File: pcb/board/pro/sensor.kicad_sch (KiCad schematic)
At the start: 2 parts, among them U1 AH49HSC

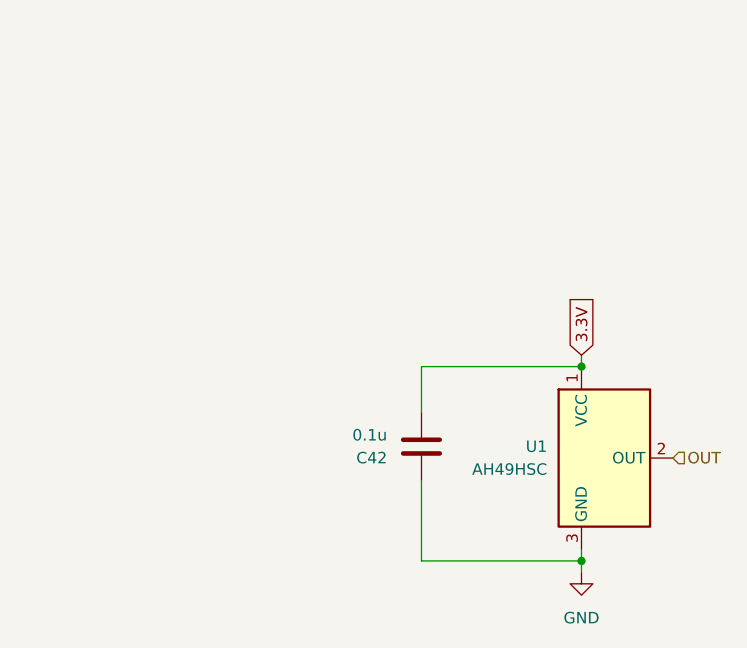
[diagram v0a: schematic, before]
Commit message: Update PCB with HSE oscillator, Footprint Mismatch fix and Rename project files to Wonkle (#36)
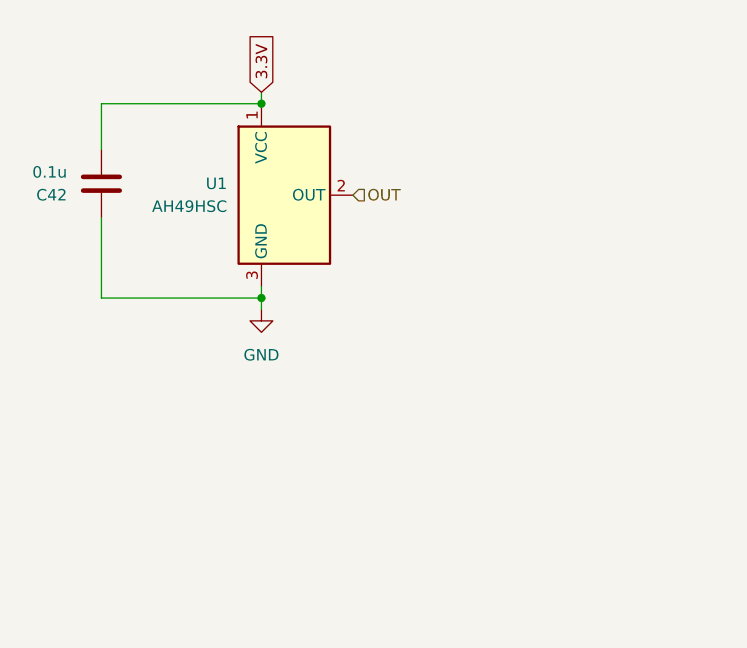
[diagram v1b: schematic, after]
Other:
- moved on the sheet: C42, U1
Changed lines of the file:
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@@
 (kicad_sch
-	(version 20250114)
+	(version 20260306)
 	(generator "eeschema")
-	(generator_version "9.0")
-	(paper "A5")
+	(generator_version "10.0")
+	(paper "User" 135 110)
 	(junction
-		(at 104.14 80.01)
+		(at 68.58 50.8)
 		(diameter 0)
 		(color 0 0 0 0)
 	)
 	(junction
-		(at 104.14 58.42)
+		(at 68.58 29.21)
 		(diameter 0)
 		(color 0 0 0 0)
@@
 	(wire
 		(pts
-			(xy 104.14 80.01) (xy 104.14 78.74)
+			(xy 68.58 50.8) (xy 68.58 49.53)
 		)
 		(stroke
@@
 	(wire
 		(pts
-			(xy 86.36 58.42) (xy 104.14 58.42)
+			(xy 50.8 29.21) (xy 68.58 29.21)
 		)
 		(stroke
@@
 	(wire
 		(pts
-			(xy 104.14 57.15) (xy 104.14 58.42)
+			(xy 68.58 27.94) (xy 68.58 29.21)
 		)
 		(stroke
@@
 	(wire
 		(pts
-			(xy 86.36 80.01) (xy 104.14 80.01)
+			(xy 50.8 50.8) (xy 68.58 50.8)
 		)
 		(stroke
@@
 	(wire
 		(pts
-			(xy 86.36 71.12) (xy 86.36 80.01)
+			(xy 50.8 41.91) (xy 50.8 50.8)
 		)
 		(stroke
@@
 	(wire
 		(pts
-			(xy 104.14 81.28) (xy 104.14 80.01)
+			(xy 68.58 52.07) (xy 68.58 50.8)
 		)
 		(stroke
@@
 	(wire
 		(pts
-			(xy 86.36 63.5) (xy 86.36 58.42)
+			(xy 50.8 34.29) (xy 50.8 29.21)
 		)
 		(stroke
@@
 	(global_label "3.3V"
 		(shape input)
-		(at 104.14 57.15 90)
+		(at 68.58 27.94 90)
 		(fields_autoplaced yes)
 		(effects
@@
 		)
 		(property "Intersheetrefs" "${INTERSHEET_REFS}"
-			(at 104.14 50.0524 90)
+			(at 68.58 20.8424 90)
+			(hide yes)
+			(show_name no)
+			(do_not_autoplace no)
 			(effects
 				(font
@@
 				)
 				(justify left)
-				(hide yes)
 			)
 		)
@@
 	(hierarchical_label "OUT"
 		(shape input)
-		(at 114.3 68.58 0)
+		(at 78.74 39.37 0)
 		(effects
 			(font
@@
 	(symbol
 		(lib_id "Device:C")
-		(at 86.36 67.31 180)
+		(at 50.8 38.1 180)
 		(unit 1)
+		(body_style 1)
 		(exclude_from_sim no)
 		(in_bom yes)
 		(on_board yes)
+		(in_pos_files yes)
 		(dnp no)
 		(property "Reference" "C42"
-			(at 82.55 68.5801 0)
+			(at 46.99 39.3701 0)
+			(show_name no)
+			(do_not_autoplace no)
 			(effects
 				(font
@@
 		)
 		(property "Value" "0.1u"
-			(at 82.55 66.0401 0)
+			(at 46.99 36.8301 0)
+			(show_name no)
+			(do_not_autoplace no)
 			(effects
 				(font
@@
 		)
 		(property "Footprint" "Capacitor_SMD:C_0402_1005Metric"
-			(at 85.3948 63.5 0)
+			(at 49.8348 34.29 0)
+			(hide yes)
+			(show_name no)
+			(do_not_autoplace no)
 			(effects
 				(font
 					(size 1.27 1.27)
 				)
-				(hide yes)
-			)
-		)
-		(property "Datasheet" "~"
-			(at 86.36 67.31 0)
+			)
+		)
+		(property "Datasheet" ""
+			(at 50.8 38.1 0)
+			(hide yes)
+			(show_name no)
+			(do_not_autoplace no)
 			(effects
 				(font
 					(size 1.27 1.27)
 				)
-				(hide yes)
 			)
 		)
 		(property "Description" "Unpolarized capacitor"
-			(at 86.36 67.31 0)
+			(at 50.8 38.1 0)
+			(hide yes)
+			(show_name no)
+			(do_not_autoplace no)
 			(effects
 				(font
 					(size 1.27 1.27)
 				)
-				(hide yes)
 			)
 		)
 		(property "LCSC Part #" "C1525"
-			(at 86.36 67.31 0)
+			(at 50.8 38.1 0)
+			(hide yes)
+			(show_name no)
+			(do_not_autoplace no)
 			(effects
 				(font
 					(size 1.27 1.27)
 				)
-				(hide yes)
 			)
 		)
@@
 		)
 		(instances
-			(project "pompyboard"
+			(project "Wonkle"
 				(path "/e5830f2e-b6bc-440e-bdf9-7651ab21e3a0/026cd3d2-ee49-4aa8-a6be-1ded8cec01b6/04e242d3-4b8b-4c59-b96a-ded88d9c121e"
 					(reference "C123")
@@
 	(symbol
 		(lib_id "Sensor_Magnetic:DRV5055A4xDBZxQ1")
-		(at 106.68 68.58 0)
+		(at 71.12 39.37 0)
 		(unit 1)
+		(body_style 1)
 		(exclude_from_sim no)
 		(in_bom yes)
 		(on_board yes)
+		(in_pos_files yes)
 		(dnp no)
 		(fields_autoplaced yes)
 		(property "Reference" "U1"
-			(at 100.33 67.3099 0)
+			(at 64.77 38.0999 0)
+			(show_name no)
+			(do_not_autoplace no)
 			(effects
 				(font
@@
 		)
 		(property "Value" "AH49HSC"
-			(at 100.33 69.8499 0)
+			(at 64.77 40.6399 0)
+			(show_name no)
+			(do_not_autoplace no)
 			(effects
 				(font
@@
 		)
 		(property "Footprint" "Package_TO_SOT_SMD:SOT-23-3"
-			(at 106.68 68.58 0)
+			(at 71.12 39.37 0)
+			(hide yes)
+			(show_name no)
+			(do_not_autoplace no)
 			(effects
 				(font
 					(size 1.27 1.27)
 				)
-				(hide yes)
 			)
 		)
 		(property "Datasheet" ""
-			(at 106.68 68.58 0)
+			(at 71.12 39.37 0)
+			(hide yes)
+			(show_name no)
+			(do_not_autoplace no)
 			(effects
 				(font
 					(size 1.27 1.27)
 				)
-				(hide yes)
 			)
 		)
 		(property "Description" ""
-			(at 106.68 68.58 0)
+			(at 71.12 39.37 0)
+			(hide yes)
+			(show_name no)
+			(do_not_autoplace no)
 			(effects
 				(font
 					(size 1.27 1.27)
 				)
-				(hide yes)
 			)
 		)
 		(property "LCSC Part #" "C510723"
-			(at 106.68 68.58 0)
+			(at 71.12 39.37 0)
+			(hide yes)
+			(show_name no)
+			(do_not_autoplace no)
 			(effects
 				(font
 					(size 1.27 1.27)
 				)
-				(hide yes)
 			)
 		)
@@
 		)
 		(instances
-			(project "pompyboard"
+			(project "Wonkle"
 				(path "/e5830f2e-b6bc-440e-bdf9-7651ab21e3a0/026cd3d2-ee49-4aa8-a6be-1ded8cec01b6/04e242d3-4b8b-4c59-b96a-ded88d9c121e"
 					(reference "U141")
@@
 	(symbol
 		(lib_id "power:GND")
-		(at 104.14 81.28 0)
+		(at 68.58 52.07 0)
 		(unit 1)
+		(body_style 1)
 		(exclude_from_sim no)
 		(in_bom yes)
 		(on_board yes)
+		(in_pos_files yes)
 		(dnp no)
 		(fields_autoplaced yes)
 		(property "Reference" "#PWR040"
-			(at 104.14 87.63 0)
+			(at 68.58 58.42 0)
+			(hide yes)
+			(show_name no)
+			(do_not_autoplace no)
 			(effects
 				(font
 					(size 1.27 1.27)
 				)
-				(hide yes)
 			)
 		)
 		(property "Value" "GND"
-			(at 104.14 86.36 0)
+			(at 68.58 57.15 0)
+			(show_name no)
+			(do_not_autoplace no)
 			(effects
 				(font
@@
 		)
 		(property "Footprint" ""
-			(at 104.14 81.28 0)
+			(at 68.58 52.07 0)
+			(hide yes)
+			(show_name no)
+			(do_not_autoplace no)
 			(effects
 				(font
 					(size 1.27 1.27)
 				)
-				(hide yes)
 			)
 		)
 		(property "Datasheet" ""
-			(at 104.14 81.28 0)
+			(at 68.58 52.07 0)
+			(hide yes)
+			(show_name no)
+			(do_not_autoplace no)
 			(effects
 				(font
 					(size 1.27 1.27)
 				)
-				(hide yes)
 			)
 		)
 		(property "Description" "Power symbol creates a global label with name \"GND\" , ground"
-			(at 104.14 81.28 0)
+			(at 68.58 52.07 0)
+			(hide yes)
+			(show_name no)
+			(do_not_autoplace no)
 			(effects
 				(font
 					(size 1.27 1.27)
 				)
-				(hide yes)
 			)
 		)
@@
 		)
 		(instances
-			(project "pompyboard"
+			(project "Wonkle"
 				(path "/e5830f2e-b6bc-440e-bdf9-7651ab21e3a0/026cd3d2-ee49-4aa8-a6be-1ded8cec01b6/04e242d3-4b8b-4c59-b96a-ded88d9c121e"
 					(reference "#PWR0202")
